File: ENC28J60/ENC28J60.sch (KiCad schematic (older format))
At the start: 23 parts, among them IC1 ENC28J60-I/SP, J1 RJ45-TRANSFO, X1 25Mhz

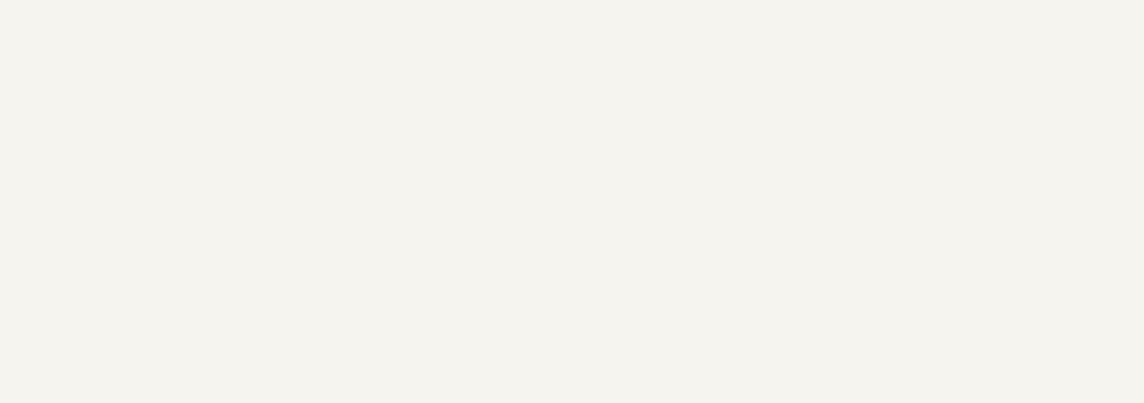
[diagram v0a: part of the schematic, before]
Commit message: added CreativeCommons License
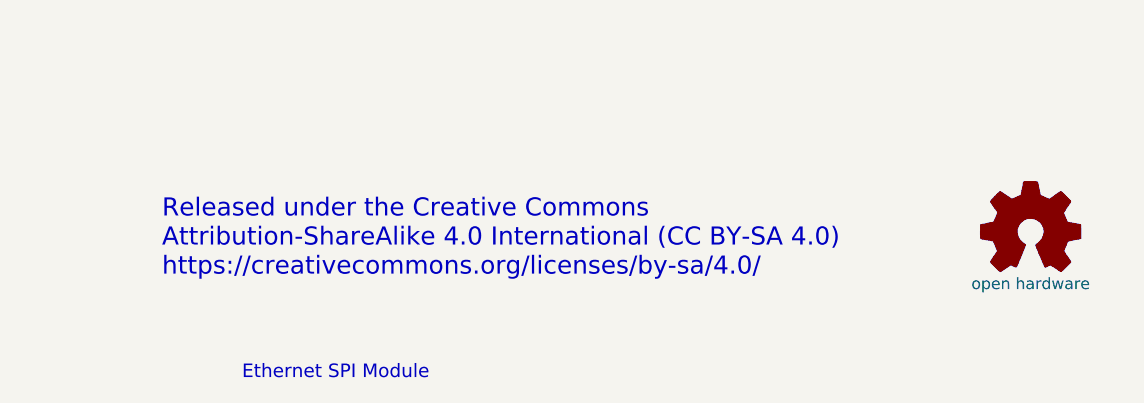
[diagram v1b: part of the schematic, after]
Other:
- note added: "Ethernet SPI Module"
- note added: "Released under the Creative Commons\nAttribution-ShareAlike 4.0 International (CC BY-SA 4.0) \nhttps://creativecommons.org/licenses/by-sa/4.0/"
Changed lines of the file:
@@
 LIBS:contrib
 LIBS:valves
+LIBS:graphic_symbols
+LIBS:ENC28J60-cache
 EELAYER 25 0
 EELAYER END
@@
 Wire Wire Line
 	6300 3200 5400 3200
+Text Notes 7050 7050 0    79   ~ 0
+Released under the Creative Commons\nAttribution-ShareAlike 4.0 International (CC BY-SA 4.0) \nhttps://creativecommons.org/licenses/by-sa/4.0/
+$Comp
+L Logo_Open_Hardware_Small #LOGO?
+U 1 1 59A1FAC2
+P 10850 6850
+F 0 "#LOGO?" H 10850 7125 50  0001 C CNN
+F 1 "open hardware" H 10850 6625 50  0000 C CNN
+F 2 "" H 10850 6850 50  0001 C CNN
+F 3 "" H 10850 6850 50  0001 C CNN
+	1    10850 6850
+	1    0    0    -1
+$EndComp
+Text Notes 7400 7500 0    59   ~ 0
+Ethernet SPI Module
 $EndSCHEMATC
